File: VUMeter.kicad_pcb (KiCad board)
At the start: 2 copper layers, 34.3 x 30.5 mm, 20 parts, among them J1 Conn_01x04_Male, U1 LM3915

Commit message: update parts
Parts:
- C1, C2, C3: footprint Capacitor_THT:CP_Radial_D6.3mm_P2.50mm -> Capacitor_THT:CP_Radial_D5.0mm_P2.50mm
- D1, D10, D2, D3, D4, D5, D6, D7, D8, D9: footprint LED_THT:LED_Rectangular_W3.9mm_H1.9mm -> LED_THT:LED_Rectangular_W5.0mm_H2.0mm
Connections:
- U1 pad 9: (no net) -> Net-(U1-Pad9)

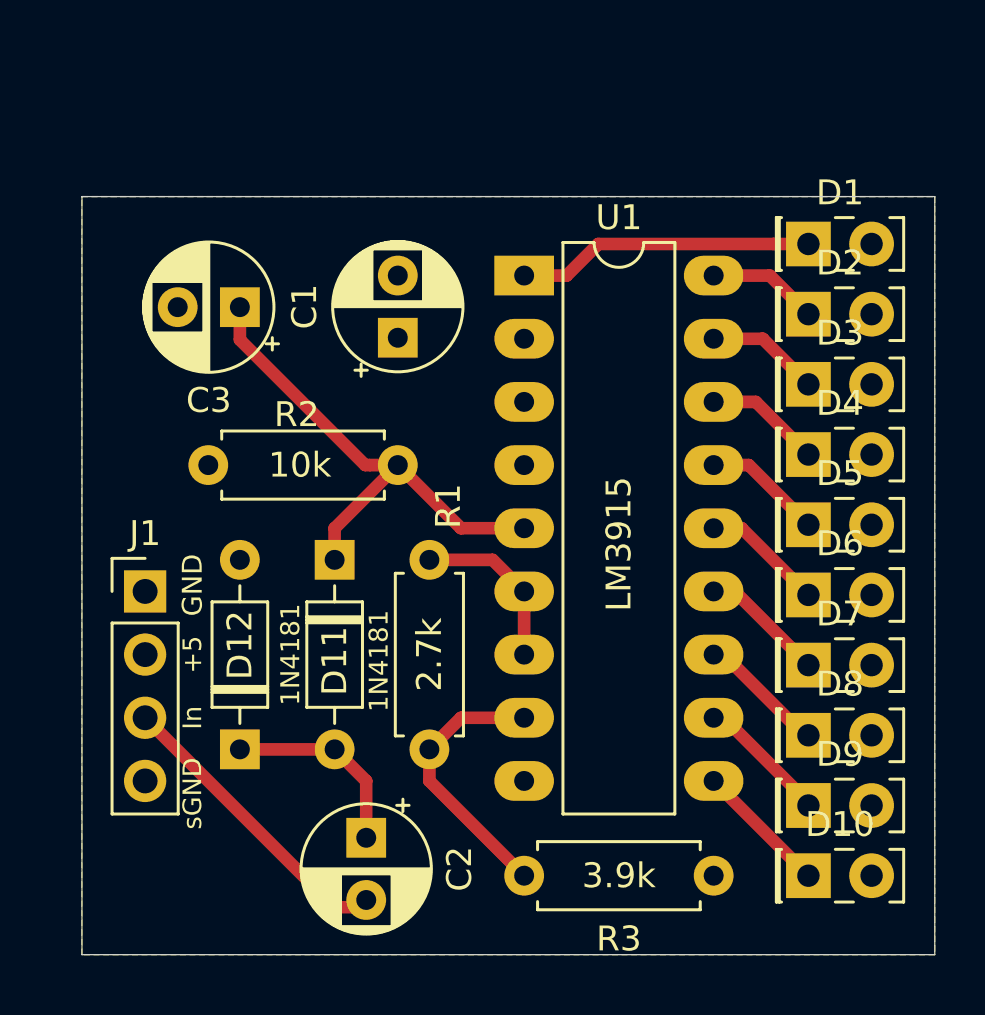
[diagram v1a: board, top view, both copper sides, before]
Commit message: update for new PCB layout
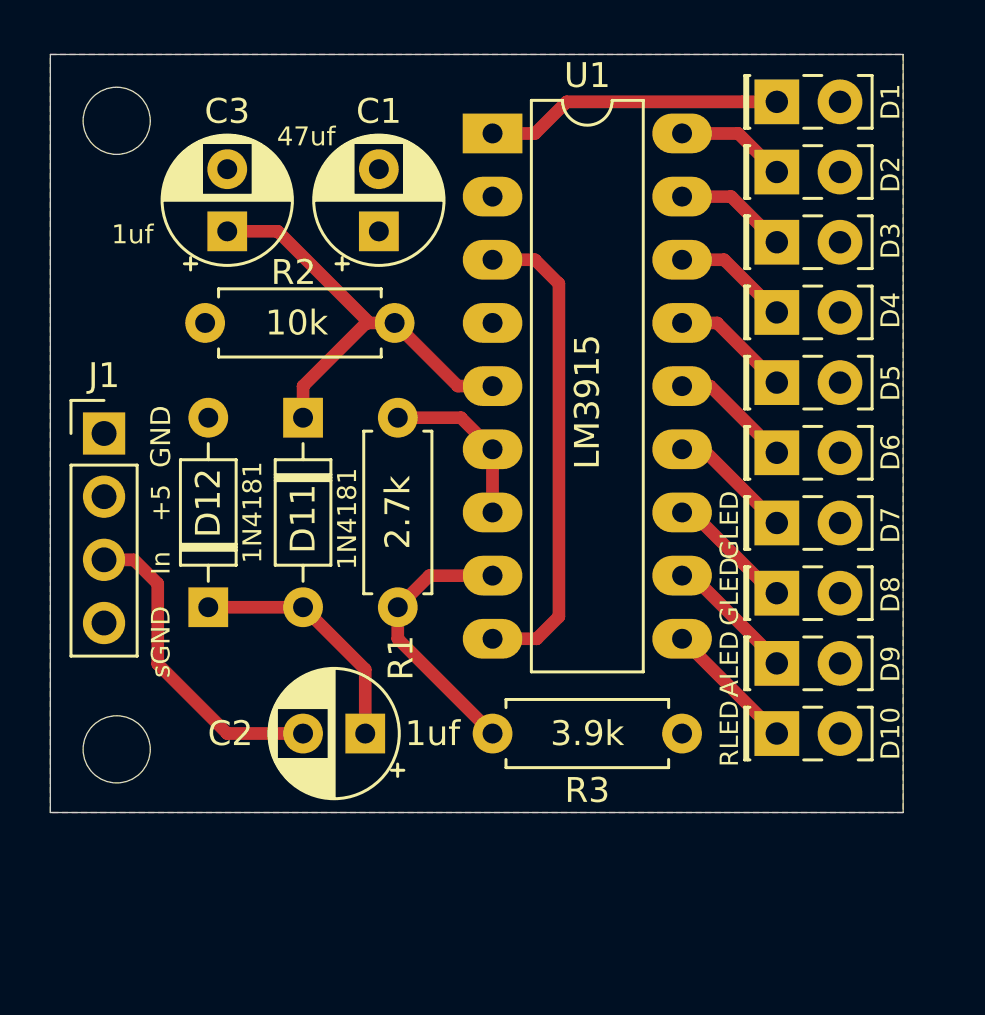
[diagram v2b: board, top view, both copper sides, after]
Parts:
- added H1: MountingHole, MountingHole:MountingHole_2.7mm_M2.5_DIN965, F.Cu at (66.2, 91.4)
- added H2: MountingHole, MountingHole:MountingHole_2.7mm_M2.5_DIN965, F.Cu at (66.2, 66.2)
- D1, D2, D3, D4, D5, D6, D7: value LED -> GLED
- D10: value LED -> RLED
- D8, D9: value LED -> ALED
- moved J1 6.56 mm to (65.7, 78.7)
- moved D1 5.85 mm to (92.7, 65.4)
- moved D12 5.85 mm to (69.8, 85.7)
- moved D2 5.85 mm to (92.7, 68.2)
- moved D3 5.85 mm to (92.7, 71.0)
- moved D5 5.85 mm to (92.7, 76.7)
- moved D6 5.85 mm to (92.7, 79.5)
- moved D7 5.85 mm to (92.7, 82.3)
- moved D9 5.85 mm to (92.7, 88.0)
- moved U1 5.85 mm to (81.3, 66.7)
- moved D10 5.85 mm to (92.7, 90.8)
- moved D11 5.85 mm to (73.7, 78.1)
- moved D4 5.85 mm to (92.7, 73.9)
- moved D8 5.85 mm to (92.7, 85.2)
- moved R1 5.85 mm to (77.5, 78.1)
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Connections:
- U1 pad 9: Net-(U1-Pad9) -> +5V
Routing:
- net +5V: track 0.00 -> 19.5 mm
- net Net-(C3-Pad1): track 20.7 -> 18.2 mm
- net Net-(C2-Pad1): track 8.19 -> 9.93 mm
- net Net-(C2-Pad2): track 12.0 -> 12.8 mm
